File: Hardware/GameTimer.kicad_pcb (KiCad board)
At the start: 2 copper layers, 55 x 16 mm, 51 parts

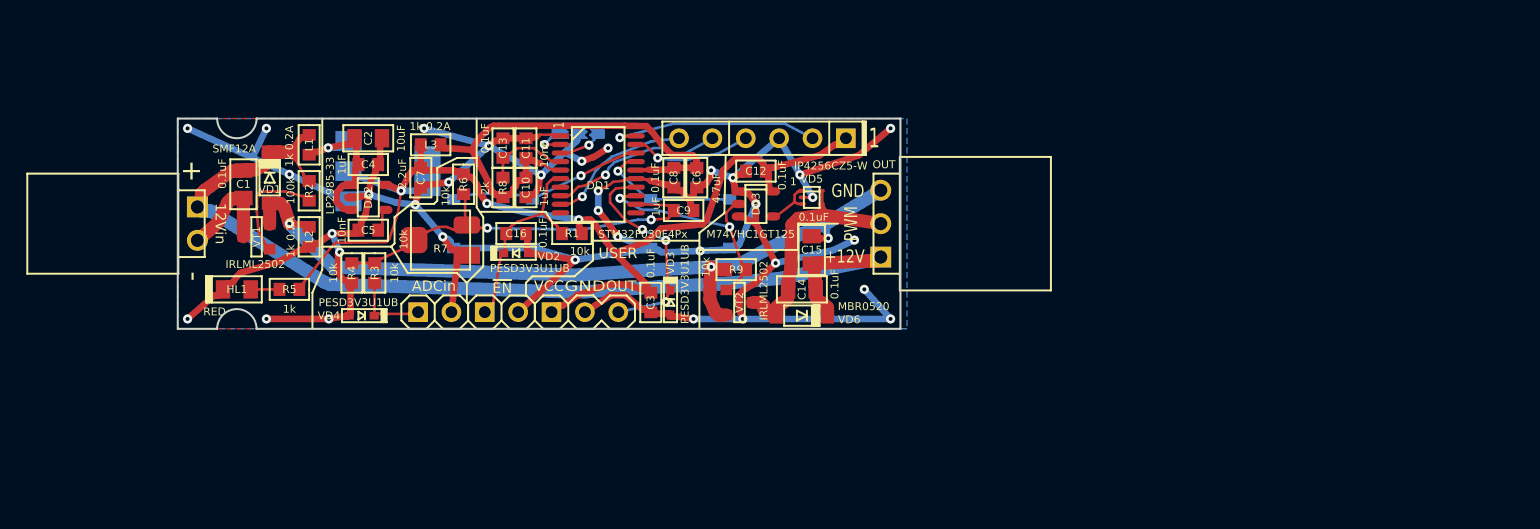
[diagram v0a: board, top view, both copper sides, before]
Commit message: Таймер для игрушек: примерная схема
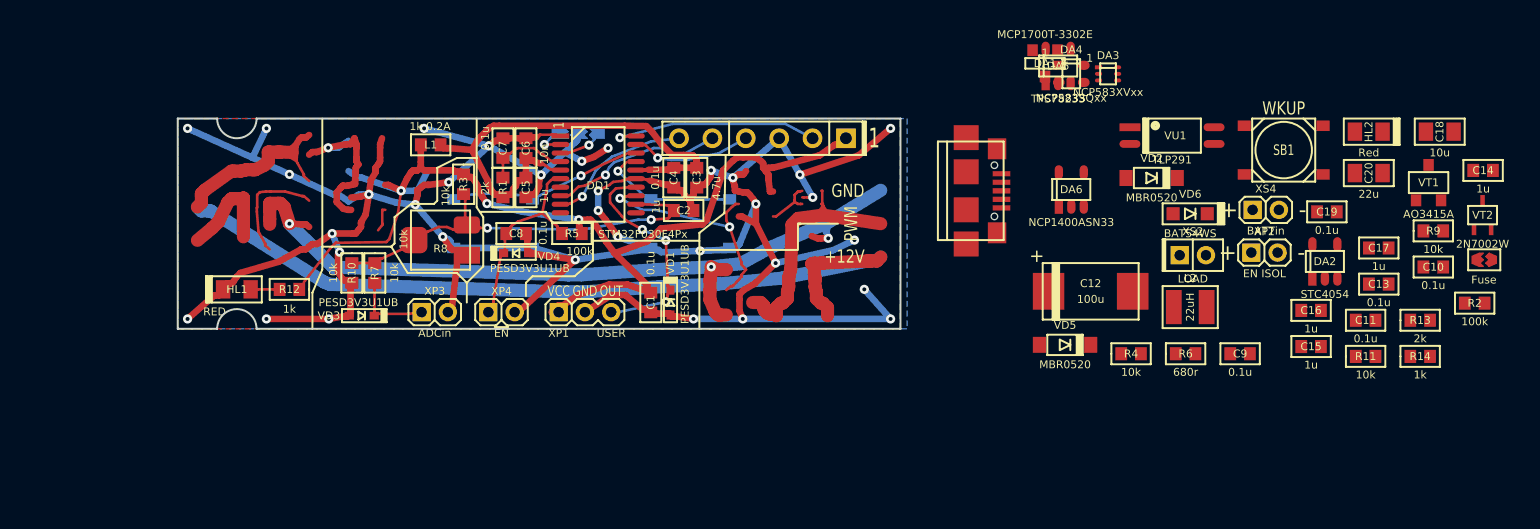
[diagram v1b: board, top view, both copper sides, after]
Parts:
- removed the C1 at (105.0, 55.0)
- removed the C2 at (114.5, 51.5)
- removed the C4 at (114.5, 53.5)
- removed the C5 at (114.5, 58.5)
- removed the C7 at (118.5, 54.5)
- removed the L1 at (110.0, 52.0)
- removed the VD1 at (107.0, 54.5)
- removed XP5: OUT, Connectors:MX2.54-3R
- added C10: 0.1u, Capacitors:CAP0603, F.Cu at (195.6, 61.3)
- added C11: 0.1u, Capacitors:CAP0603, F.Cu at (190.4, 65.3)
- added C13: 0.1u, Capacitors:CAP0603, F.Cu at (191.4, 62.6)
- added C16: 1u, Capacitors:CAP0603, F.Cu at (186.3, 64.6)
- added C17: 1u, Capacitors:CAP0603, F.Cu at (191.4, 59.9)
- added C18: 10u, Capacitors:CAP0805, F.Cu at (196.0, 51.0)
- added C19: 0.1u, Capacitors:CAP0603, F.Cu at (187.5, 57.1)
- added C20: 22u, Capacitors:CAP0805, F.Cu at (190.6, 54.1)
- added C9: 0.1u, Capacitors:CAP0603, F.Cu at (180.9, 67.9)
- added DA4: NCP583SQxx, SOT,_TO:SC82AB, F.Cu at (168.0, 46.6)
- added DA5: TPS78233, SOT,_TO:SOT23-5, F.Cu at (167.0, 46.0)
- added DA6: NCP1400ASN33, SOT,_TO:SOT23-5, F.Cu at (168.0, 55.4)
- added HL2: Red, LEDs:LED0805, F.Cu at (190.6, 51.0)
- added R11: 10k, Resistors:RES0603, F.Cu at (190.4, 68.1)
- added R13: 2k, Resistors:RES0603, F.Cu at (194.6, 65.3)
- added R14: 1k, Resistors:RES0603, F.Cu at (194.6, 68.1)
- added R4: 10k, Resistors:RES0603, F.Cu at (172.6, 67.9)
- added R6: 680r, Resistors:RES0603, F.Cu at (176.7, 67.9)
- added SB1: WKUP, Buttons,_Switches:BTN_5x5(AJ-037), F.Cu at (184.2, 52.4)
- added VD2: MBR0520, Diodes:SOD123, F.Cu at (174.1, 54.5)
- added VU1: TLP291, Opto:opto_SOP4, F.Cu at (175.7, 51.3)
- added XS2: LOAD, Connectors:PBS2-2, F.Cu at (177.3, 60.4)
- added XS3: USB-micro B, Connectors:USB-micro_B, F.Cu at (160.0, 55.5)
- added XS4: BATTin, Connectors:for_PolarOut_PLS2-2, F.Cu at (182.8, 57.0)
- added fus2: Fuse, PCB_details:FuseSolder, F.Cu at (199.4, 60.8)
- C1: renamed from C3; value 0.1uF -> 0.1u
- C12: value 0.1uF -> 100u; footprint Capacitors:CAP0603 -> Capacitors:CAP_pol_SMD-7343
- C14, C15: value 0.1uF -> 1u; footprint Capacitors:CAP0805 -> Capacitors:CAP0603
- C2: renamed from C9; value 1uF -> 1u
- C3: renamed from C6; value 4.7uF -> 4.7u
- C4: renamed from C8; value 0.1uF -> 0.1u
- C5: renamed from C10; value 1uF -> 1u
- C6: renamed from C11; value 10nF -> 10n
- C7: renamed from C13; value 0.1uF -> 0.1u
- C8: renamed from C16; value 0.1uF -> 0.1u
- DA1: value TLV1117-33 -> MCP1700T-3302E; footprint SOT,_TO:SOT223 -> SOT,_TO:SOT23-3; moved to F.Cu
- DA2: value LP2985-33 -> STC4054
- DA3: value M74VHC1GT125 -> NCP583XVxx; footprint SOT,_TO:SOT23-5 -> SOT,_TO:SOT563
- L2: value 1k 0.2A -> 22uH; footprint Inductors:Bead_0603 -> Inductors:IND1210_LQH32C
- R5: renamed from R1; value 10k -> 100k
- VD5: value IP4256CZ5-W -> MBR0520; footprint SOT,_TO:SOT553 -> Diodes:SOD123
- VD6: value MBR0520 -> BAT54WS; footprint Diodes:SOD123 -> Diodes:SOD323
- VT1: value IRLML2502 -> AO3415A; footprint SOT,_TO:SOT23-3 -> SOT,_TO:SOT23A
- VT2: value IRLML2502 -> 2N7002W; footprint SOT,_TO:SOT23-3 -> SOT,_TO:SOT323
- XP1: value 12Vin -> USER; footprint Connectors:for_PolarOut_MX2.54-2R -> Connectors:for_SENS_PLS2-3
- XP2: value ~EN -> EN ISOL; footprint Connectors:PLS-2 -> Connectors:for_PolarOut_PLS2-2
- XP3: value USER -> ADCin; footprint Connectors:for_SENS_PLS-3 -> Connectors:PLS2-2
- XP4: value ADCin -> ~EN; footprint Connectors:PLS-2 -> Connectors:PLS2-2
- moved VT1 89.3 mm to (195.2, 54.9), turned to 0 degrees
- moved R2 89.1 mm to (198.7, 64.0), turned to 0 degrees
- moved DA2 73.0 mm to (187.3, 60.9), turned to 0 degrees
- moved L2 67.3 mm to (177.1, 64.3), turned to 0 degrees
- moved XP2 58.2 mm to (182.7, 60.2)
- moved VT2 56.9 mm to (199.3, 57.3), turned to 0 degrees
- moved R9 53.1 mm to (195.6, 58.5), turned to 0 degrees
- moved C14 52.6 mm to (199.3, 54.0), turned to 0 degrees
- moved DA1 50.7 mm to (166.0, 45.8), turned to 180 degrees
- moved C15 38.7 mm to (186.3, 67.3), turned to 0 degrees
- moved VD6 30.5 mm to (177.1, 57.2), turned to 0 degrees
- moved XP1 30.2 mm to (131.0, 64.7), turned to 0 degrees
- moved DA3 28.6 mm to (170.8, 46.6), turned to 0 degrees
- moved C12 27.1 mm to (169.5, 63.1), turned to 0 degrees
- moved VD5 22.3 mm to (167.5, 67.2)
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- renumbered L3 to L1, R8 to R1, R4 to R10, R5 to R12, R6 to R3, R3 to R7, R7 to R8, SB1 to SB3, VD3 to VD1, VD4 to VD3, VD2 to VD4
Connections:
- C12 pad 1: +3.3V -> +BATT
- C14 pad 1: +12Vin -> /+USBvcc
- C14 pad 2: /PWM_OUT -> GND
- C15 pad 1: +12Vin -> +BATT
- C15 pad 2: GNDP -> GND
- DA1 pad 3: +12V -> +BATT
- DA2 pad 1: +12V -> /Chg_STAT
- DA2 pad 3: +12V -> +BATT
- DA2 pad 4: Net-(C5-Pad1) -> /+USBvcc
- DA2 pad 5: +3.3V -> Net-(DA2-Pad5)
- DA3 pad 1: GND -> +BATT
- DA3 pad 2: /PWM -> GND
- DA3 pad 3: GND -> +3.3V
- DA3 pad 4: Net-(DA3-Pad4) -> (no net)
- DA3 pad 5: +3.3V -> GND
- DD1 pad 10: (no net) -> /BTN1
- DD1 pad 11: (no net) -> /BTN2
- DD1 pad 17: /BTN1 -> (no net)
- DD1 pad 18: /BTN2 -> (no net)
- DD1 pad 7: (no net) -> /MEAS_EN
- L2 pad 1: GNDP -> /+LOAD_OUT
- L2 pad 2: GND -> /LX1
- R12 pad 1: +3.3V -> /PWM
- R2 pad 1: +12Vin -> +BATT
- R2 pad 2: Net-(R2-Pad2) -> /switch
- R7 pad 2: Net-(R3-Pad2) -> Net-(R7-Pad2)
- R8 pad 1: GND -> /MEAS_EN
- R9 pad 2: GNDP -> GND
- VD3 pad C: Net-(R3-Pad2) -> Net-(R7-Pad2)
- VD6 pad A: /PWM_OUT -> /switch
- VD6 pad C: +12Vin -> /EN_WKUP
- VT1 pad 1: Net-(R2-Pad2) -> /switch
- VT1 pad 2: GNDP -> +BATT
- VT1 pad 3: /GNDin -> /+LOAD_OUT
- VT2 pad 2: GNDP -> GND
- VT2 pad 3: /PWM_OUT -> /switch
- XP1 pad 1: +12Vin -> +3.3V
- XP1 pad 2: /GNDin -> GND
- XP2 pad 1: /EN_WKUP -> Net-(R6-Pad2)
- XP2 pad 2: GND -> Net-(VU1-Pad2)
- XP3 pad 1: +3.3V -> Net-(R7-Pad2)
- XP4 pad 1: Net-(R3-Pad2) -> /EN_WKUP
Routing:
- net +BATT: track 0.00 -> 12.9 mm, vias 0 -> 1
- net +12V: track 12.9 -> 0.00 mm, vias 1 -> 0
- net Net-(R7-Pad2): track 0.00 -> 5.89 mm
- net Net-(R3-Pad2): track 5.89 -> 0.00 mm
- net GND: track 230.7 -> 228.3 mm
- net /BTN2: track 14.9 -> 14.2 mm
- net /BTN1: track 11.0 -> 10.3 mm
- net +3.3V: track 81.1 -> 80.4 mm

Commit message: Игровой таймер: расстановка компонентов наяата
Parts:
- removed the DA3 at (170.8, 46.6)
- removed the DA4 at (168.0, 46.6)
- removed the R5 at (130.0, 58.8)
- removed fus2: Fuse, PCB_details:FuseSolder
- added R1: 100k, Resistors:RES0603, F.Cu at (125.0, 59.0)
- added XP5: 5Vin, Connectors:for_PolarOut_PLS2-2, F.Cu at (108.0, 65.0)
- C16: renamed from C13; moved to B.Cu
- C17: renamed from C14; moved to B.Cu
- C18: renamed from C15; moved to B.Cu
- DA1: value MCP1700T-3302E -> MCP1700T
- DA3: renamed from DA2; moved to B.Cu
- HL2: moved to B.Cu
- R14: renamed from R13; moved to B.Cu
- R15: renamed from R14; moved to B.Cu
- SB2: renamed from SB1; value WKUP -> ON/WKUP
- XS4: renamed from XS3; moved to B.Cu
- moved C17 89.6 mm to (109.8, 55.5)
- moved R14 89.4 mm to (106.0, 53.0), turned to 270 degrees
- moved C1 86.7 mm to (104.5, 53.5), turned to 270 degrees
- moved C16 84.7 mm to (106.8, 59.5), turned to 90 degrees
- moved R15 82.5 mm to (113.0, 55.5), turned to 180 degrees
- moved XS1 81.9 mm to (101.0, 52.0), turned to 270 degrees
- moved C20 79.4 mm to (112.5, 51.2)
- moved HL2 78.9 mm to (112.0, 57.5)
- moved DA3 77.9 mm to (109.8, 53.0), turned to 270 degrees
- moved C19 74.0 mm to (112.5, 58.8)
- moved C18 73.9 mm to (113.8, 53.0), turned to 90 degrees
- moved SB2 66.0 mm to (121.2, 72.2)
- moved C2 62.8 mm to (106.8, 59.2), turned to 270 degrees
- moved C12 62.8 mm to (132.8, 60.0)
- moved XS4 58.6 mm to (101.5, 59.5)
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- renumbered C11 to C1, C7 to C10, C9 to C11, C10 to C12, C18 to C13, C19 to C14, C20 to C15, C16 to C19, C12 to C2, C17 to C20, C8 to C3, C1 to C4, C2 to C5, C3 to C6, C4 to C7, C5 to C8, C6 to C9, DA6 to DA2, DA5 to DA4, R8 to R10, R10 to R11, R11 to R12, R12 to R13, R1 to R2, R2 to R3, R6 to R4, R3 to R5, R4 to R6, R7 to R8, SB2 to SB1, VD6 to VD3, VD3 to VD4, VD4 to VD5, VD5 to VD6, XS4 to XS1, XS1 to XS2, XS2 to XS3
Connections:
- net /PWM renamed /LoadCtrl
- DD1 pad 12: /ADC -> /USER
- DD1 pad 14: /USER -> /ADC
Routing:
- net +12Vin: track 80.3 -> 0.00 mm
- net GND: track 228.3 -> 154.8 mm, vias 34 -> 24
- net GNDP: track 62.7 -> 0.00 mm, vias 3 -> 0
- net +3.3V: track 80.4 -> 32.9 mm, vias 3 -> 2
- net /PWM_OUT: track 20.2 -> 0.00 mm
- net +BATT: track 12.9 -> 0.00 mm, vias 1 -> 0
- net Net-(R2-Pad2): track 8.66 -> 0.00 mm
- net /GNDin: track 8.09 -> 0.00 mm
- net /LoadCtrl: track 18.1 -> 12.3 mm
- net Net-(DA3-Pad4): track 3.88 -> 0.00 mm
- net /ADC: track 31.3 -> 28.9 mm
- net Net-(HL1-PadA): track 2.20 -> 0.00 mm
- net Net-(C5-Pad1): track 1.89 -> 0.00 mm
- net /USER: track 16.6 -> 15.0 mm

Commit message: Игровой таймер: компоненты расставлены
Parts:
- removed the SB1 at (124.0, 58.0)
- removed SB3: Up, Buttons,_Switches:BTN_5x5(AJ-037)
- added C21: 0.1u, Capacitors:CAP0603, B.Cu at (136.5, 61.8)
- added VD7: PESD3V3U1UB, Diodes:SOD523, B.Cu at (138.8, 56.5)
- added fus2: Out | Vin, PCB_details:FuseSolder_x2_0603, B.Cu at (130.0, 61.8)
- C13, C14, C15, DA2, L2, R4, VD6, VU1: moved to B.Cu
- HL2, R15: moved to F.Cu
- SB1: renamed from SB2; moved to B.Cu
- moved R3 56.1 mm to (143.0, 57.0), turned to 90 degrees
- moved VT2 52.6 mm to (146.8, 60.2), turned to 270 degrees
- moved R9 52.6 mm to (143.0, 60.2), turned to 270 degrees
- moved HL1 52.5 mm to (153.8, 52.5), turned to 90 degrees
- moved C15 51.2 mm to (140.5, 64.8), turned to 180 degrees
- moved R13 50.2 mm to (151.0, 53.8), turned to 0 degrees
- moved VT1 48.5 mm to (146.8, 57.0), turned to 270 degrees
- moved C14 46.2 mm to (141.5, 62.0), turned to 90 degrees
- moved C13 44.1 mm to (153.5, 62.8), turned to 270 degrees
- moved Logo1 32.5 mm to (125.0, 55.2), turned to 270 degrees
- moved VD3 31.9 mm to (145.8, 63.5)
- moved L2 24.1 mm to (150.5, 63.0), turned to 270 degrees
- moved DA2 23.6 mm to (146.0, 62.5), turned to 90 degrees
- moved VD6 21.6 mm to (146.0, 65.0), turned to 180 degrees
- moved R4 18.0 mm to (136.5, 59.5), turned to 180 degrees
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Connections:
- C12 pad 1: /USER -> /BATT_MEAS
- C4 pad 1: +3.3V -> /+USER_VCC
- DD1 pad 10: /BTN1 -> (no net)
- DD1 pad 11: /BTN2 -> /BATT_MEAS
- DD1 pad 12: /USER -> /LoadCtrl
- DD1 pad 13: /LoadCtrl -> /USER
- R12 pad 1: /USER -> /BATT_MEAS
- R6 pad 2: /USER -> /BATT_MEAS
- XP1 pad 1: +3.3V -> /+USER_VCC
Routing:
- net GND: track 154.8 -> 82.2 mm, vias 24 -> 16
- net +3.3V: track 32.9 -> 0.00 mm, vias 2 -> 0
- net /ADC: track 28.9 -> 1.92 mm, vias 2 -> 0
- net /EN_WKUP: track 15.4 -> 0.00 mm
- net /LoadCtrl: track 12.3 -> 0.00 mm, vias 2 -> 0
- net Net-(C21-Pad2): track 0.00 -> 10.3 mm, vias 0 -> 1
- net /BTN1: track 10.3 -> 0.00 mm, vias 1 -> 0
- net /SWCLK: track 16.3 -> 12.1 mm, vias 1 -> 0
- net Net-(R8-Pad2): track 5.89 -> 2.50 mm
- net /USER: track 15.0 -> 12.1 mm, vias 3 -> 2
- net /+MSU_PWR: track 39.8 -> 37.3 mm
- net /Mode2: track 3.58 -> 2.87 mm
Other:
- board text added: "+"
- board text added: "-"
- board text added: "5Vin"
- board text added: "BATTin"
- board text added: "PESD3V3"
- board text added: "USER VCC"
- board text added: "«Game Timer»"
- board text removed: "+12V"
- board text removed: "12Vin"
- board text removed: "PWM"
- board text removed: "instead 2985"
- board text removed: "«PWM Regulator»"

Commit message: GameTimer: работа завершена
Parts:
- moved C12 4.25 mm to (134.2, 59.0), turned to 180 degrees
- moved R6 4.25 mm to (138.5, 59.0), turned to 180 degrees
- moved fus1 1.75 mm to (132.0, 51.0)
- moved C19 0.50 mm to (113.0, 59.2)
- moved C20 0.50 mm to (113.0, 51.8)
- moved DA1 0.50 mm to (112.0, 55.4)
- moved DA4 0.50 mm to (113.0, 55.5)
- moved C8 0.25 mm to (126.5, 55.5)
- moved R11 0.25 mm to (112.2, 62.0)
- moved R2 0.25 mm to (124.2, 55.5)
- moved R8 0.25 mm to (114.0, 62.0)
- moved VD4 0.25 mm to (113.0, 65.2)
- turned R1 to 0 degrees
- turned R5 to 180 degrees
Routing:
- net GND: track 82.2 -> 285.8 mm, vias 16 -> 38
- net +BATT: track 0.00 -> 67.3 mm, vias 0 -> 2
- net +3.3V: track 0.00 -> 64.5 mm, vias 0 -> 3
- net /EN_WKUP: track 0.00 -> 61.8 mm, vias 0 -> 3
- net /+LOAD_OUT: track 0.00 -> 38.3 mm, vias 0 -> 3
- net /+USBvcc: track 0.00 -> 37.1 mm
- net /ADC: track 1.92 -> 38.1 mm, vias 0 -> 2
- net /LoadCtrl: track 0.00 -> 21.3 mm, vias 0 -> 2
- net /MEAS_EN: track 0.00 -> 21.0 mm, vias 0 -> 3
- net /Chg_STAT: track 0.00 -> 15.7 mm, vias 0 -> 1
- net /BTN2: track 14.2 -> 0.00 mm, vias 1 -> 0
- net /switch: track 0.00 -> 12.5 mm
- net /BATT_MEAS: track 0.00 -> 9.58 mm
- net /+MSU_PWR: track 37.3 -> 43.8 mm
- net /+USER_VCC: track 0.00 -> 5.97 mm
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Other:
- rule pad_to_mask_clearance: 0.2 -> 0
- board text added: "Start for Wkup btn"
